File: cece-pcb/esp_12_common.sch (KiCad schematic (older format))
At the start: 26 parts, among them Q1 Q_NPN, SW1 RES, U1 ESP-12F

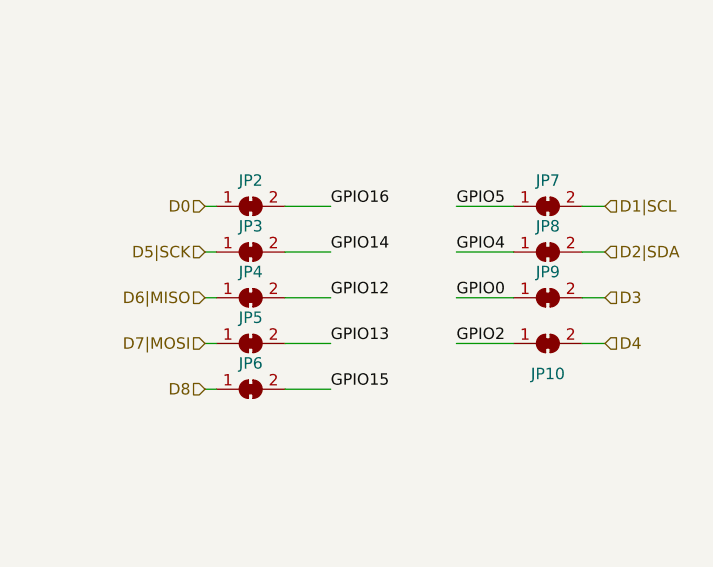
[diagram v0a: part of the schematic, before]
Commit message: Complete ESP-12 part of the PCB
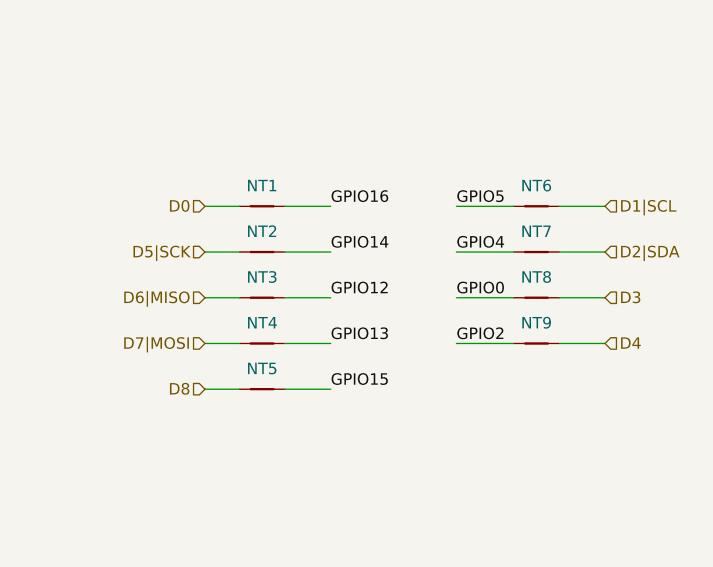
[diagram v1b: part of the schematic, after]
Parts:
- removed JP10: D4/GPIO2, Jumper:SolderJumper-2_P1.3mm_Bridged_Pad1.0x1.5mm, symbol Jumper:SolderJumper_2_Bridged
- removed JP2: D0/GPIO16, Jumper:SolderJumper-2_P1.3mm_Bridged_Pad1.0x1.5mm, symbol Jumper:SolderJumper_2_Bridged
- removed JP3: D5/GPIO14, Jumper:SolderJumper-2_P1.3mm_Bridged_Pad1.0x1.5mm, symbol Jumper:SolderJumper_2_Bridged
- removed JP4: D6/GPIO12, Jumper:SolderJumper-2_P1.3mm_Bridged_Pad1.0x1.5mm, symbol Jumper:SolderJumper_2_Bridged
- removed JP5: D7/GPIO13, Jumper:SolderJumper-2_P1.3mm_Bridged_Pad1.0x1.5mm, symbol Jumper:SolderJumper_2_Bridged
- removed JP6: D8/GPIO15, Jumper:SolderJumper-2_P1.3mm_Bridged_Pad1.0x1.5mm, symbol Jumper:SolderJumper_2_Bridged
- removed JP7: D1/GPIO5, Jumper:SolderJumper-2_P1.3mm_Bridged_Pad1.0x1.5mm, symbol Jumper:SolderJumper_2_Bridged
- removed JP8: D2/GPIO4, Jumper:SolderJumper-2_P1.3mm_Bridged_Pad1.0x1.5mm, symbol Jumper:SolderJumper_2_Bridged
- removed JP9: D3/GPIO0, Jumper:SolderJumper-2_P1.3mm_Bridged_Pad1.0x1.5mm, symbol Jumper:SolderJumper_2_Bridged
- added NT1: D0/GPIO16, NetTie:NetTie-2_SMD_Pad0.5mm, symbol Device:Net-Tie_2
- added NT2: D5/GPIO14, NetTie:NetTie-2_SMD_Pad0.5mm, symbol Device:Net-Tie_2
- added NT3: D6/GPIO12, NetTie:NetTie-2_SMD_Pad0.5mm, symbol Device:Net-Tie_2
- added NT4: D7/GPIO13, NetTie:NetTie-2_SMD_Pad0.5mm, symbol Device:Net-Tie_2
- added NT5: D8/GPIO15, NetTie:NetTie-2_SMD_Pad0.5mm, symbol Device:Net-Tie_2
- added NT6: D1/GPIO5, NetTie:NetTie-2_SMD_Pad0.5mm, symbol Device:Net-Tie_2
- added NT7: D2/GPIO4, NetTie:NetTie-2_SMD_Pad0.5mm, symbol Device:Net-Tie_2
- added NT8: D3/GPIO0, NetTie:NetTie-2_SMD_Pad0.5mm, symbol Device:Net-Tie_2
- added NT9: D4/GPIO2, NetTie:NetTie-2_SMD_Pad0.5mm, symbol Device:Net-Tie_2
- U1: footprint ESP8266:ESP-12E_SMD -> ESP8266:ESP-12E
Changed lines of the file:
@@
 Text HLabel 7250 3900 2    50   Input ~ 0
 RX
-$Comp
-L Jumper:SolderJumper_2_Bridged JP2
-U 1 1 5FC406E6
-P 7850 2000
-F 0 "JP2" H 7850 2113 50  0000 C CNN
-F 1 "D0/GPIO16" H 7850 2114 50  0001 C CNN
-F 2 "Jumper:SolderJumper-2_P1.3mm_Bridged_Pad1.0x1.5mm" H 7850 2000 50  0001 C CNN
-F 3 "~" H 7850 2000 50  0001 C CNN
-	1    7850 2000
-	1    0    0    -1
-$EndComp
-$Comp
-L Jumper:SolderJumper_2_Bridged JP3
-U 1 1 5FC41135
-P 7850 2200
-F 0 "JP3" H 7850 2313 50  0000 C CNN
-F 1 "D5/GPIO14" H 7850 2314 50  0001 C CNN
-F 2 "Jumper:SolderJumper-2_P1.3mm_Bridged_Pad1.0x1.5mm" H 7850 2200 50  0001 C CNN
-F 3 "~" H 7850 2200 50  0001 C CNN
-	1    7850 2200
-	1    0    0    -1
-$EndComp
-$Comp
-L Jumper:SolderJumper_2_Bridged JP4
-U 1 1 5FC4170D
-P 7850 2400
-F 0 "JP4" H 7850 2513 50  0000 C CNN
-F 1 "D6/GPIO12" H 7850 2514 50  0001 C CNN
-F 2 "Jumper:SolderJumper-2_P1.3mm_Bridged_Pad1.0x1.5mm" H 7850 2400 50  0001 C CNN
-F 3 "~" H 7850 2400 50  0001 C CNN
-	1    7850 2400
-	1    0    0    -1
-$EndComp
-$Comp
-L Jumper:SolderJumper_2_Bridged JP5
-U 1 1 5FC41AF4
-P 7850 2600
-F 0 "JP5" H 7850 2713 50  0000 C CNN
-F 1 "D7/GPIO13" H 7850 2714 50  0001 C CNN
-F 2 "Jumper:SolderJumper-2_P1.3mm_Bridged_Pad1.0x1.5mm" H 7850 2600 50  0001 C CNN
-F 3 "~" H 7850 2600 50  0001 C CNN
-	1    7850 2600
-	1    0    0    -1
-$EndComp
-Wire Wire Line
-	7700 2000 7650 2000
-Wire Wire Line
-	7700 2200 7650 2200
-Wire Wire Line
-	7700 2400 7650 2400
-Wire Wire Line
-	7700 2600 7650 2600
 Wire Wire Line
 	4950 4600 4950 4500
-$Comp
-L Jumper:SolderJumper_2_Bridged JP7
-U 1 1 5FC7D052
-P 9150 2000
-F 0 "JP7" H 9150 2113 50  0000 C CNN
-F 1 "D1/GPIO5" H 9150 2114 50  0001 C CNN
-F 2 "Jumper:SolderJumper-2_P1.3mm_Bridged_Pad1.0x1.5mm" H 9150 2000 50  0001 C CNN
-F 3 "~" H 9150 2000 50  0001 C CNN
-	1    9150 2000
-	1    0    0    -1
-$EndComp
-$Comp
-L Jumper:SolderJumper_2_Bridged JP8
-U 1 1 5FC7E515
-P 9150 2200
-F 0 "JP8" H 9150 2313 50  0000 C CNN
-F 1 "D2/GPIO4" H 9150 2314 50  0001 C CNN
-F 2 "Jumper:SolderJumper-2_P1.3mm_Bridged_Pad1.0x1.5mm" H 9150 2200 50  0001 C CNN
-F 3 "~" H 9150 2200 50  0001 C CNN
-	1    9150 2200
-	1    0    0    -1
-$EndComp
-$Comp
-L Jumper:SolderJumper_2_Bridged JP9
-U 1 1 5FC7EA08
-P 9150 2400
-F 0 "JP9" H 9150 2513 50  0000 C CNN
-F 1 "D3/GPIO0" H 9150 2514 50  0001 C CNN
-F 2 "Jumper:SolderJumper-2_P1.3mm_Bridged_Pad1.0x1.5mm" H 9150 2400 50  0001 C CNN
-F 3 "~" H 9150 2400 50  0001 C CNN
-	1    9150 2400
-	1    0    0    -1
-$EndComp
-$Comp
-L Jumper:SolderJumper_2_Bridged JP10
-U 1 1 5FC7F09B
-P 9150 2600
-F 0 "JP10" H 9150 2467 50  0000 C CNN
-F 1 "D4/GPIO2" H 9150 2714 50  0001 C CNN
-F 2 "Jumper:SolderJumper-2_P1.3mm_Bridged_Pad1.0x1.5mm" H 9150 2600 50  0001 C CNN
-F 3 "~" H 9150 2600 50  0001 C CNN
-	1    9150 2600
-	1    0    0    -1
-$EndComp
 Wire Wire Line
 	7250 3800 6950 3800
@@
 Wire Wire Line
 	8750 2000 9000 2000
-Wire Wire Line
-	9300 2000 9400 2000
 Text Notes 3250 6800 0    50   ~ 0
 https://www.wemos.cc/en/latest/_static/files/sch_d1_mini_v3.0.0.pdf
-Wire Wire Line
-	9300 2200 9400 2200
-Wire Wire Line
-	9300 2400 9400 2400
-Wire Wire Line
-	9300 2600 9400 2600
 Wire Wire Line
 	4950 4500 5150 4500
@@
 Text Label 8200 2800 0    50   ~ 0
 GPIO15
-$Comp
-L Jumper:SolderJumper_2_Bridged JP6
-U 1 1 5FD1EFF9
-P 7850 2800
-F 0 "JP6" H 7850 2913 50  0000 C CNN
-F 1 "D8/GPIO15" H 7850 2914 50  0001 C CNN
-F 2 "Jumper:SolderJumper-2_P1.3mm_Bridged_Pad1.0x1.5mm" H 7850 2800 50  0001 C CNN
-F 3 "~" H 7850 2800 50  0001 C CNN
-	1    7850 2800
-	1    0    0    -1
-$EndComp
 Text HLabel 7650 2800 0    50   Input ~ 0
 D8
 Wire Wire Line
-	7650 2800 7700 2800
-Wire Wire Line
 	8000 2800 8200 2800
 Wire Wire Line
@@
 	8000 2200 8200 2200
 Wire Wire Line
-	8000 2400 8200 2400
-Wire Wire Line
 	9000 2200 8750 2200
-Wire Wire Line
-	8750 2400 9000 2400
 Wire Wire Line
 	9000 2600 8750 2600
@@
 F 0 "U1" H 6050 4865 50  0000 C CNN
 F 1 "ESP-12F" H 6050 4774 50  0000 C CNN
-F 2 "ESP8266:ESP-12E_SMD" H 6050 4100 50  0001 C CNN
+F 2 "ESP8266:ESP-12E" H 6050 4100 50  0001 C CNN
 F 3 "" H 6050 4100 50  0001 C CNN
 	1    6050 4100
@@
 Wire Wire Line
 	6950 4800 6950 4850
+$Comp
+L Device:Net-Tie_2 NT1
+U 1 1 5FC7D93D
+P 7900 2000
+F 0 "NT1" H 7900 2089 50  0000 C CNN
+F 1 "D0/GPIO16" H 7900 2090 50  0001 C CNN
+F 2 "NetTie:NetTie-2_SMD_Pad0.5mm" H 7900 2000 50  0001 C CNN
+F 3 "~" H 7900 2000 50  0001 C CNN
+	1    7900 2000
+	1    0    0    -1
+$EndComp
+Wire Wire Line
+	8000 2400 8200 2400
+$Comp
+L Device:Net-Tie_2 NT2
+U 1 1 5FC808A4
+P 7900 2200
+F 0 "NT2" H 7900 2289 50  0000 C CNN
+F 1 "D5/GPIO14" H 7900 2290 50  0001 C CNN
+F 2 "NetTie:NetTie-2_SMD_Pad0.5mm" H 7900 2200 50  0001 C CNN
+F 3 "~" H 7900 2200 50  0001 C CNN
+	1    7900 2200
+	1    0    0    -1
+$EndComp
+$Comp
+L Device:Net-Tie_2 NT3
+U 1 1 5FC80AA9
+P 7900 2400
+F 0 "NT3" H 7900 2489 50  0000 C CNN
+F 1 "D6/GPIO12" H 7900 2490 50  0001 C CNN
+F 2 "NetTie:NetTie-2_SMD_Pad0.5mm" H 7900 2400 50  0001 C CNN
+F 3 "~" H 7900 2400 50  0001 C CNN
+	1    7900 2400
+	1    0    0    -1
+$EndComp
+$Comp
+L Device:Net-Tie_2 NT4
+U 1 1 5FC80D08
+P 7900 2600
+F 0 "NT4" H 7900 2689 50  0000 C CNN
+F 1 "D7/GPIO13" H 7900 2690 50  0001 C CNN
+F 2 "NetTie:NetTie-2_SMD_Pad0.5mm" H 7900 2600 50  0001 C CNN
+F 3 "~" H 7900 2600 50  0001 C CNN
+	1    7900 2600
+	1    0    0    -1
+$EndComp
+$Comp
+L Device:Net-Tie_2 NT5
+U 1 1 5FC80F66
+P 7900 2800
+F 0 "NT5" H 7900 2889 50  0000 C CNN
+F 1 "D8/GPIO15" H 7900 2890 50  0001 C CNN
+F 2 "NetTie:NetTie-2_SMD_Pad0.5mm" H 7900 2800 50  0001 C CNN
+F 3 "~" H 7900 2800 50  0001 C CNN
+	1    7900 2800
+	1    0    0    -1
+$EndComp
+$Comp
+L Device:Net-Tie_2 NT9
+U 1 1 5FC8132F
+P 9100 2600
+F 0 "NT9" H 9100 2689 50  0000 C CNN
+F 1 "D4/GPIO2" H 9100 2690 50  0001 C CNN
+F 2 "NetTie:NetTie-2_SMD_Pad0.5mm" H 9100 2600 50  0001 C CNN
+F 3 "~" H 9100 2600 50  0001 C CNN
+	1    9100 2600
+	1    0    0    -1
+$EndComp
+Wire Wire Line
+	8750 2400 9000 2400
+$Comp
+L Device:Net-Tie_2 NT8
+U 1 1 5FC81B49
+P 9100 2400
+F 0 "NT8" H 9100 2489 50  0000 C CNN
+F 1 "D3/GPIO0" H 9100 2490 50  0001 C CNN
+F 2 "NetTie:NetTie-2_SMD_Pad0.5mm" H 9100 2400 50  0001 C CNN
+F 3 "~" H 9100 2400 50  0001 C CNN
+	1    9100 2400
+	1    0    0    -1
+$EndComp
+$Comp
+L Device:Net-Tie_2 NT7
+U 1 1 5FC81DEB
+P 9100 2200
+F 0 "NT7" H 9100 2289 50  0000 C CNN
+F 1 "D2/GPIO4" H 9100 2290 50  0001 C CNN
+F 2 "NetTie:NetTie-2_SMD_Pad0.5mm" H 9100 2200 50  0001 C CNN
+F 3 "~" H 9100 2200 50  0001 C CNN
+	1    9100 2200
+	1    0    0    -1
+$EndComp
+$Comp
+L Device:Net-Tie_2 NT6
+U 1 1 5FC82063
+P 9100 2000
+F 0 "NT6" H 9100 2089 50  0000 C CNN
+F 1 "D1/GPIO5" H 9100 2090 50  0001 C CNN
+F 2 "NetTie:NetTie-2_SMD_Pad0.5mm" H 9100 2000 50  0001 C CNN
+F 3 "~" H 9100 2000 50  0001 C CNN
+	1    9100 2000
+	1    0    0    -1
+$EndComp
+Wire Wire Line
+	7650 2000 7800 2000
+Wire Wire Line
+	7650 2200 7800 2200
+Wire Wire Line
+	7650 2400 7800 2400
+Wire Wire Line
+	7650 2600 7800 2600
+Wire Wire Line
+	7650 2800 7800 2800
+Wire Wire Line
+	9200 2000 9400 2000
+Wire Wire Line
+	9200 2200 9400 2200
+Wire Wire Line
+	9200 2400 9400 2400
+Wire Wire Line
+	9200 2600 9400 2600
 $EndSCHEMATC

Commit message: Finish first board revision
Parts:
- U1: symbol ESP8266:ESP-12F -> cece-pcb-rescue:ESP-12F-ESP8266
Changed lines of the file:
@@
 GPIO15
 $Comp
-L ESP8266:ESP-12F U1
+L cece-pcb-rescue:ESP-12F-ESP8266 U1
 U 1 1 5FC176C5
 P 6050 4100
+AR Path="/5FC176C5" Ref="U1"  Part="1"
+AR Path="/5FC173C3/5FC176C5" Ref="U1"  Part="1"
 F 0 "U1" H 6050 4865 50  0000 C CNN
 F 1 "ESP-12F" H 6050 4774 50  0000 C CNN

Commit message: Add jumper to send 5V directly to the LDO if no battery is installed
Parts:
- U1: symbol cece-pcb-rescue:ESP-12F-ESP8266 -> cece-pcb-rescue:ESP-12F-ESP8266-cece-pcb-rescue
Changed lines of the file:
@@
 GPIO15
 $Comp
-L cece-pcb-rescue:ESP-12F-ESP8266 U1
+L cece-pcb-rescue:ESP-12F-ESP8266-cece-pcb-rescue U1
 U 1 1 5FC176C5
 P 6050 4100

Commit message: Fix wrong footprint for the pin headers
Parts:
- JP11: footprint Connector_PinHeader_1.27mm:PinHeader_2x01_P1.27mm_Vertical -> Connector_PinHeader_2.54mm:PinHeader_1x02_P2.54mm_Vertical
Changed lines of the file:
@@
 F 0 "JP11" V 4954 2698 50  0000 L CNN
 F 1 "PROG" V 5045 2698 50  0000 L CNN
-F 2 "Connector_PinHeader_1.27mm:PinHeader_2x01_P1.27mm_Vertical" H 5000 2650 50  0001 C CNN
+F 2 "Connector_PinHeader_2.54mm:PinHeader_1x02_P2.54mm_Vertical" H 5000 2650 50  0001 C CNN
 F 3 "~" H 5000 2650 50  0001 C CNN
 	1    5000 2650

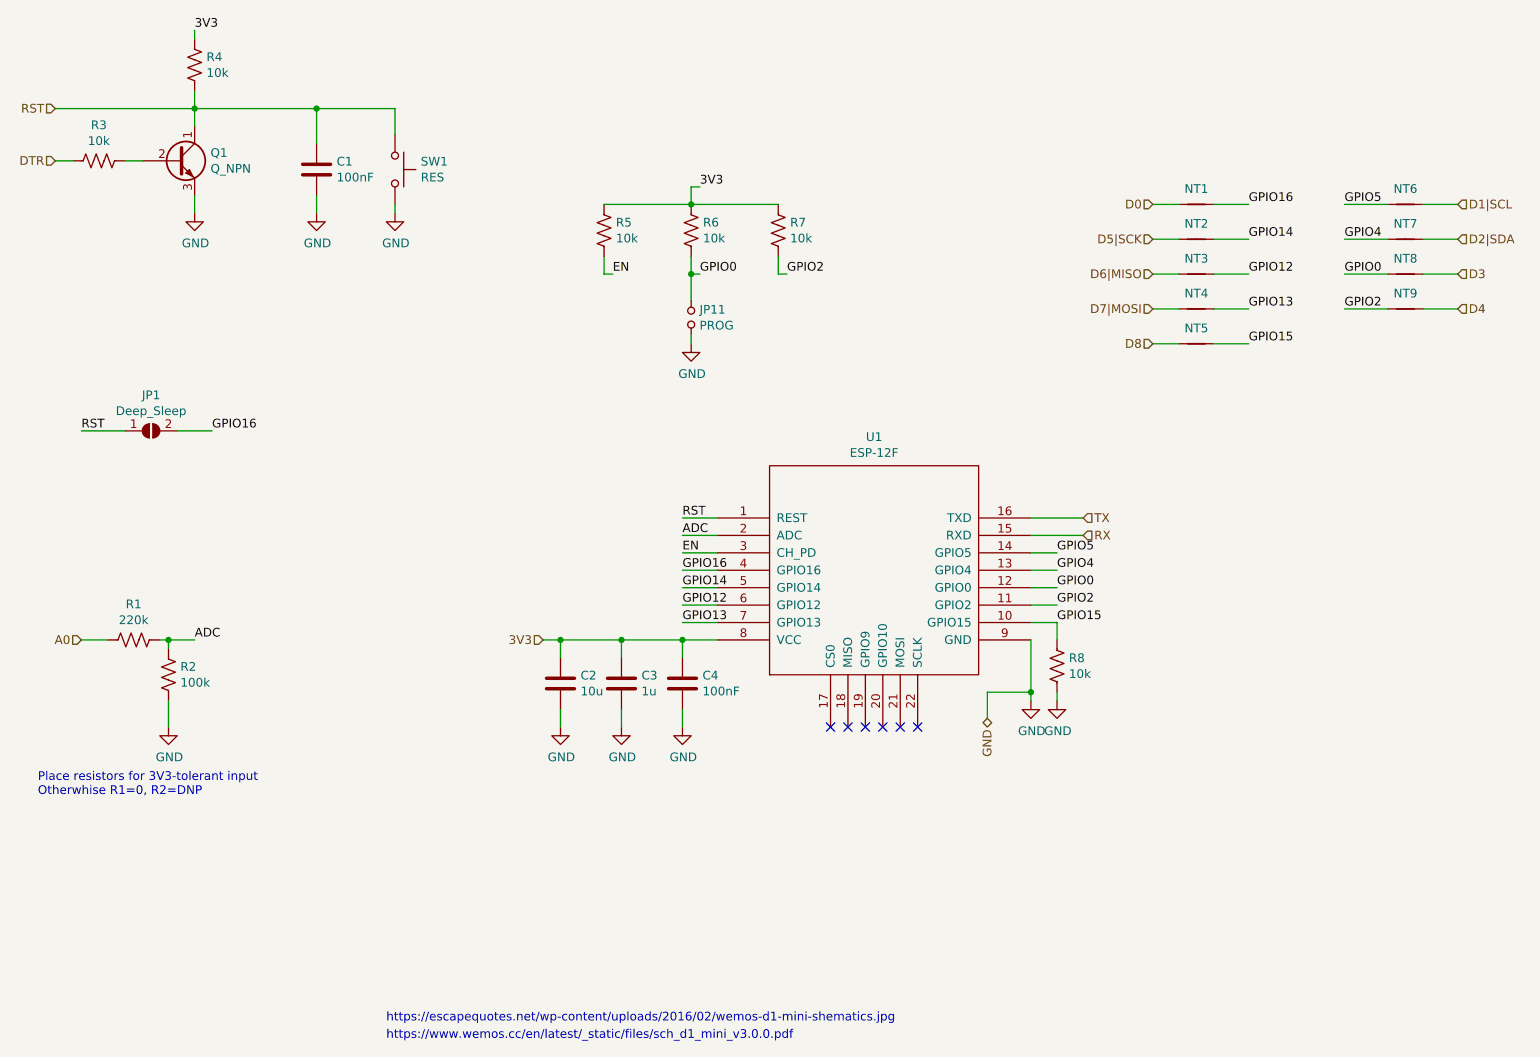
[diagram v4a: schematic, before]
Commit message: Update schematic references to reflect hierarchy
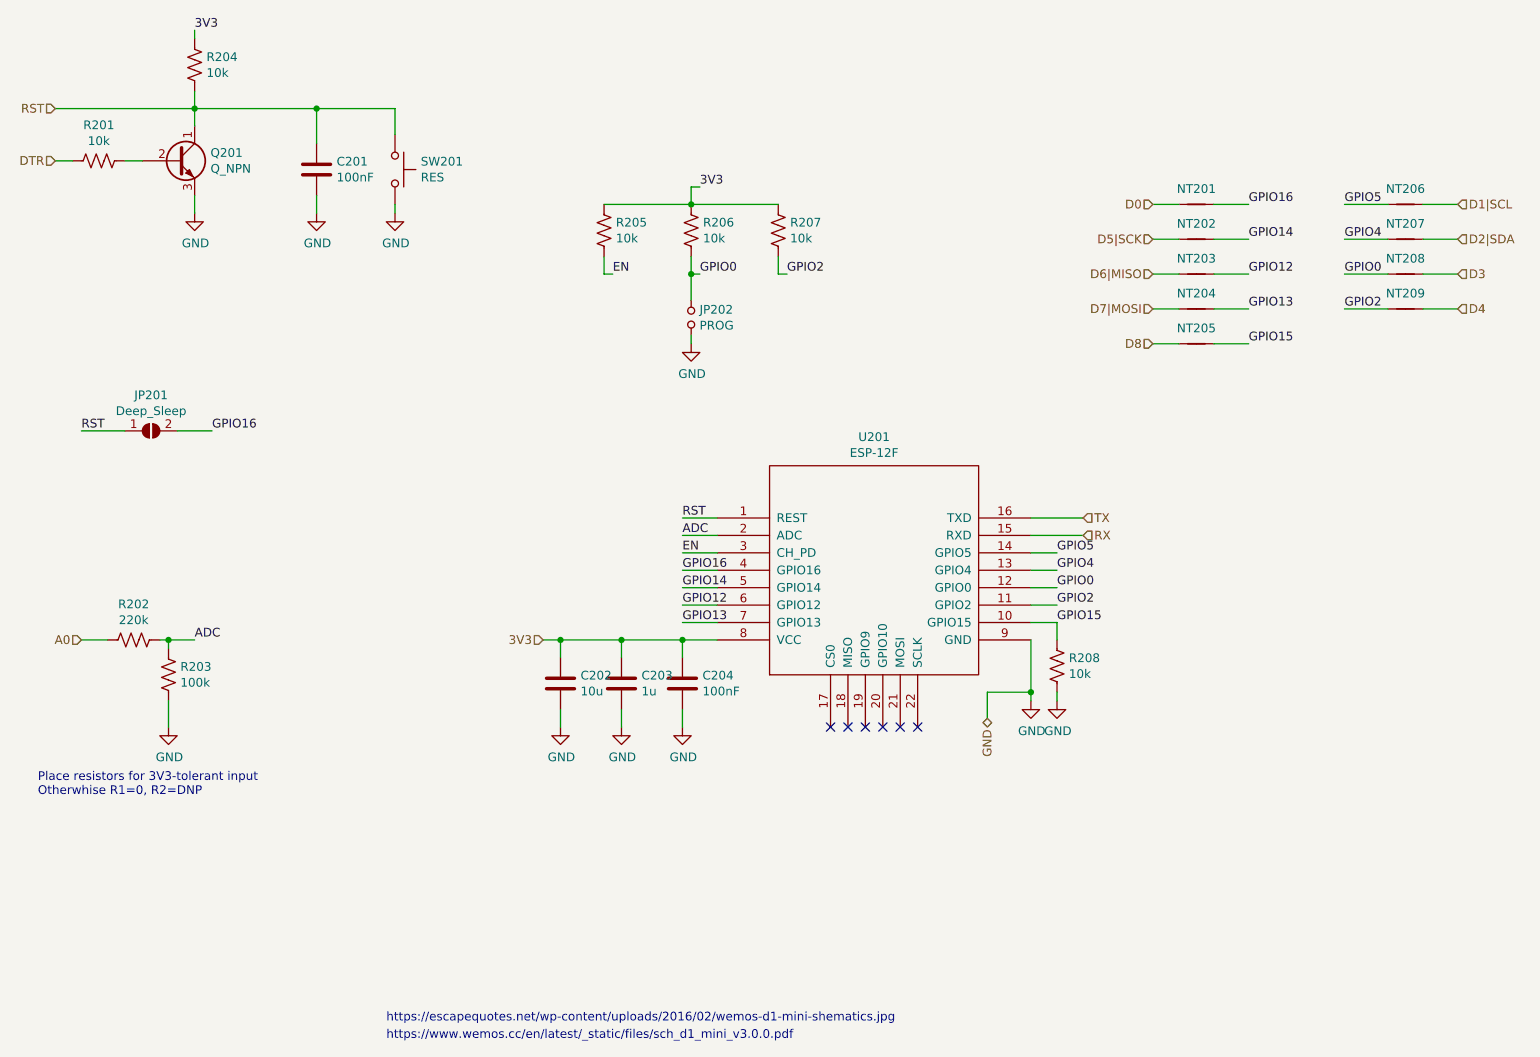
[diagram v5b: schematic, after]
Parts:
- renumbered C1 to C201, C2 to C202, C3 to C203, C4 to C204, JP1 to JP201, JP11 to JP202, NT1 to NT201, NT2 to NT202, NT3 to NT203, NT4 to NT204, NT5 to NT205, NT6 to NT206, NT7 to NT207, NT8 to NT208, NT9 to NT209, Q1 to Q201, R3 to R201, R1 to R202, R2 to R203, R4 to R204, R5 to R205, R6 to R206, R7 to R207, R8 to R208, SW1 to SW201, U1 to U201

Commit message: Boards have arrived. Fixed the many mistakes in the schematic
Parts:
- removed NT201: D0/GPIO16, NetTie:NetTie-2_SMD_Pad0.5mm, symbol Device:Net-Tie_2
- removed NT202: D5/GPIO14, NetTie:NetTie-2_SMD_Pad0.5mm, symbol Device:Net-Tie_2
- removed NT203: D6/GPIO12, NetTie:NetTie-2_SMD_Pad0.5mm, symbol Device:Net-Tie_2
- removed NT204: D7/GPIO13, NetTie:NetTie-2_SMD_Pad0.5mm, symbol Device:Net-Tie_2
- removed NT205: D8/GPIO15, NetTie:NetTie-2_SMD_Pad0.5mm, symbol Device:Net-Tie_2
- removed NT206: D1/GPIO5, NetTie:NetTie-2_SMD_Pad0.5mm, symbol Device:Net-Tie_2
- removed NT207: D2/GPIO4, NetTie:NetTie-2_SMD_Pad0.5mm, symbol Device:Net-Tie_2
- removed NT208: D3/GPIO0, NetTie:NetTie-2_SMD_Pad0.5mm, symbol Device:Net-Tie_2
- removed NT209: D4/GPIO2, NetTie:NetTie-2_SMD_Pad0.5mm, symbol Device:Net-Tie_2
- removed Q201: Q_NPN, Package_TO_SOT_THT:TO-92L_Inline_Wide, symbol Device:Q_NPN_CBE
- removed R201: 10k, Resistor_THT:R_Axial_DIN0207_L6.3mm_D2.5mm_P7.62mm_Horizontal, symbol Device:R_US
- renumbered JP202 to JP201, JP201 to JP202, R204 to R201, R205 to R202, R206 to R203, R207 to R204, R202 to R205, R208 to R206, R203 to R207
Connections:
- net GPIO0 is gone; now on net D3: JP201.1, R203.1, U201.12 (GPIO0)
- net GPIO12 is gone; now on net D6|MISO: U201.6 (GPIO12)
- net GPIO13 is gone; now on net D7|MOSI: U201.7 (GPIO13)
- net GPIO14 is gone; now on net D5|SCK: U201.5 (GPIO14)
- net GPIO15 is gone; now on net D8: R206.2, U201.10 (GPIO15)
- net GPIO16 is gone; now on net D0: JP202.2 (B), U201.4 (GPIO16)
- net GPIO2 is gone; now on net D4: R204.1, U201.11 (GPIO2)
- net GPIO4 is gone; now on net D2|SDA: U201.13 (GPIO4)
- net GPIO5 is gone; now on net D1|SCL: U201.14 (GPIO5)
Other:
- moved on the sheet: C201, JP201, R201, R202, R203, R204, SW201
